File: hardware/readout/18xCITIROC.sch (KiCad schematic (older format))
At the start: 0 parts

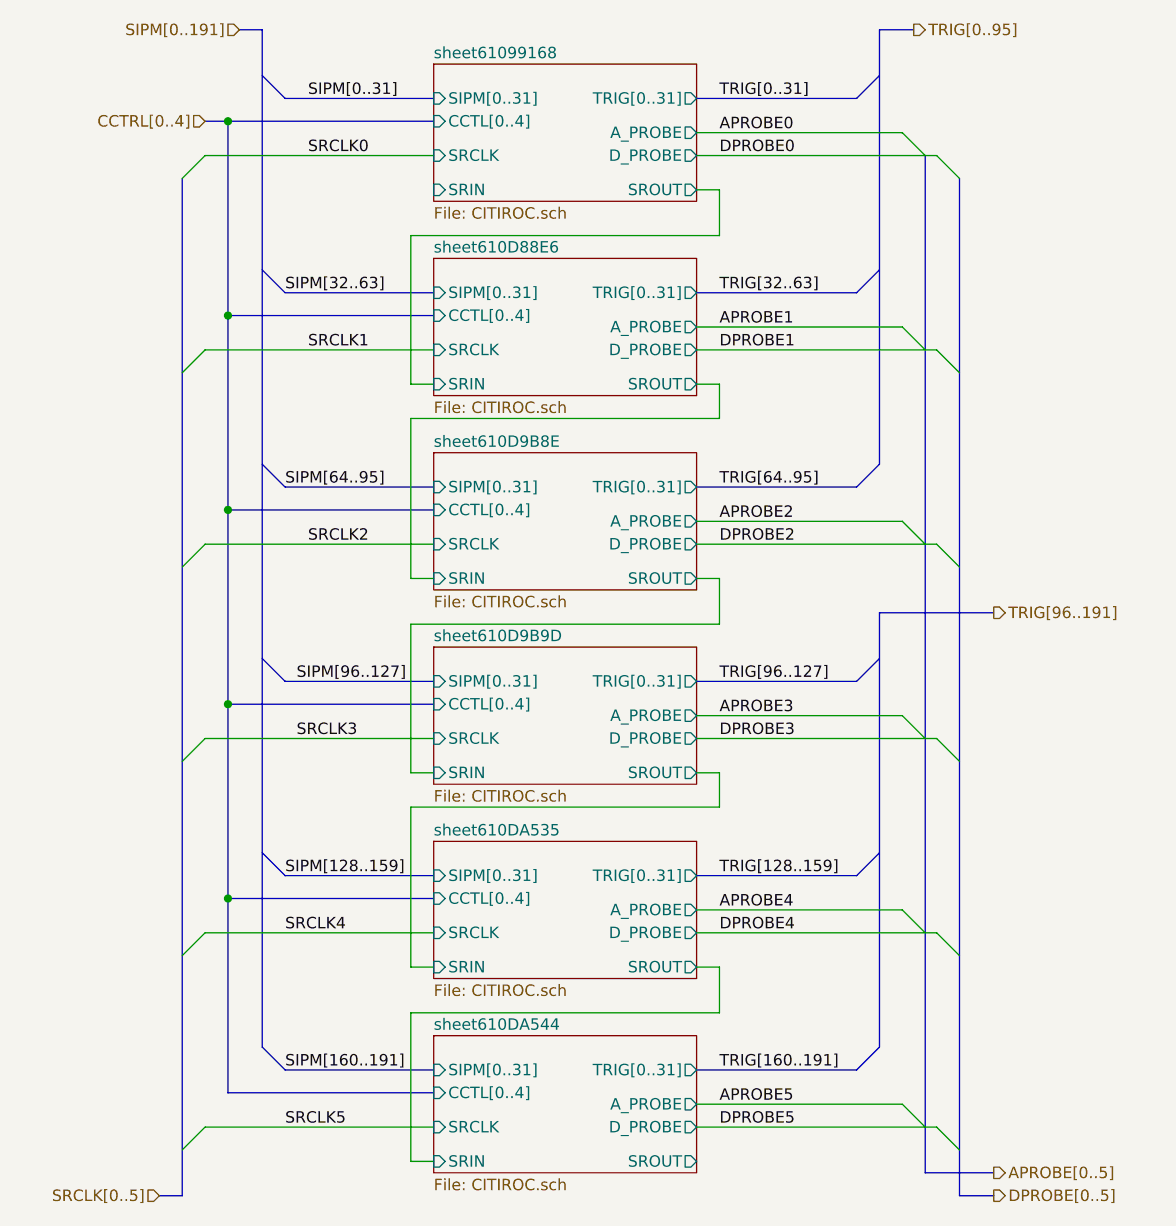
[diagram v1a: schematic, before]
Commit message: Readout schem heirarchy almost done
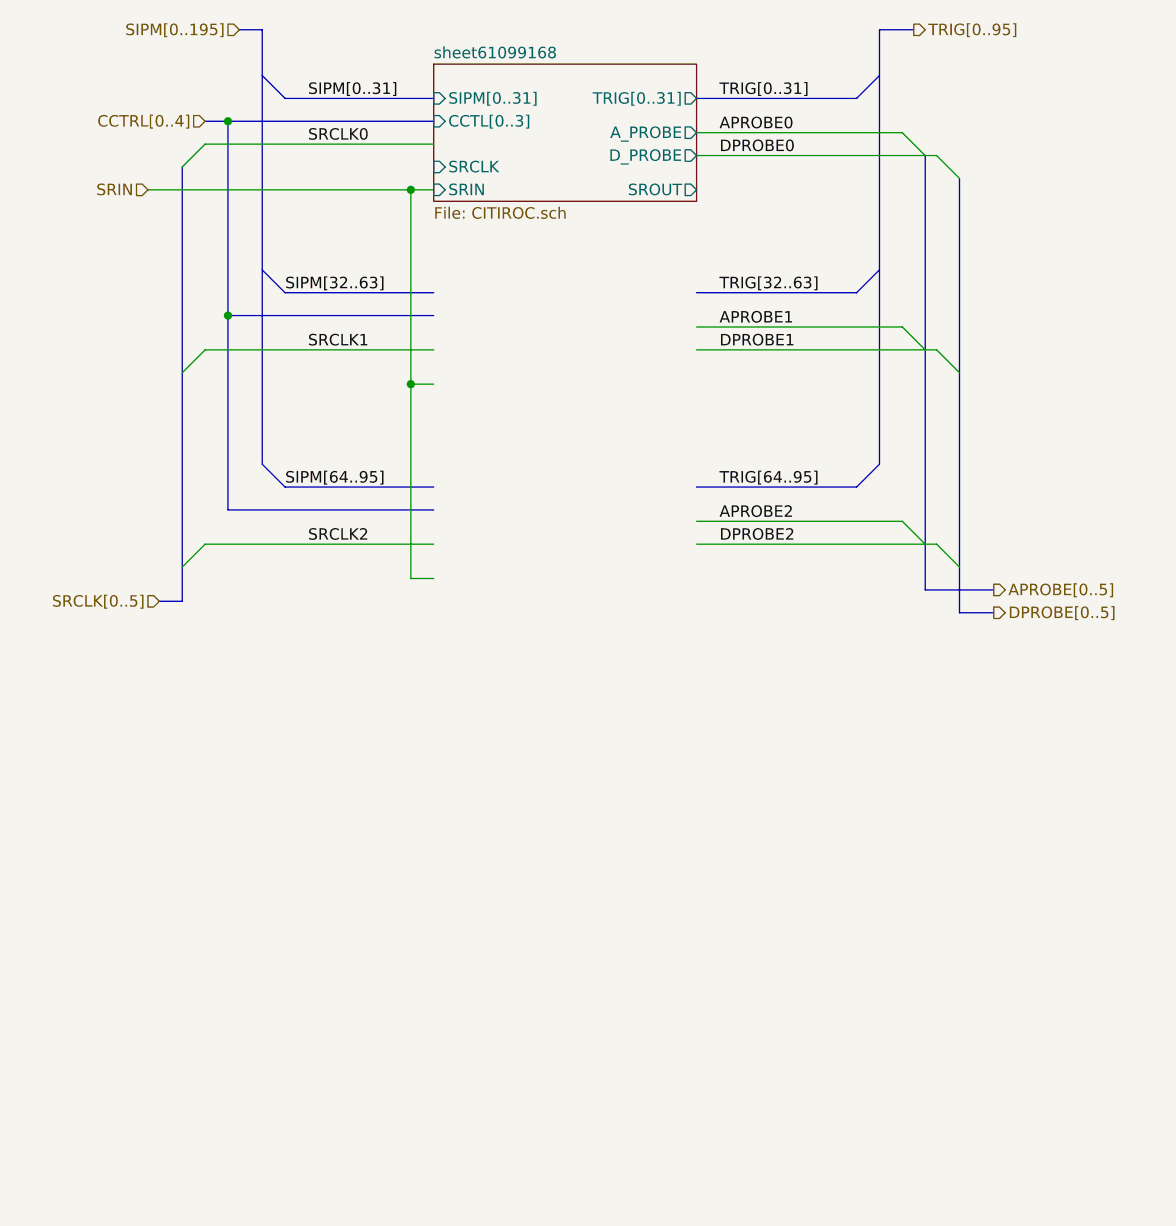
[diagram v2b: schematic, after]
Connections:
- net labels added: SIPM[0..195], SRIN
- net labels removed: APROBE3, APROBE4, APROBE5, DPROBE3, DPROBE4, DPROBE5, SIPM[0..191], SIPM[128..159], SIPM[160..191], SIPM[96..127], SRCLK3, SRCLK4, SRCLK5, TRIG[128..159], TRIG[160..191], TRIG[96..127], TRIG[96..191]
- wire segments 43 -> 15
